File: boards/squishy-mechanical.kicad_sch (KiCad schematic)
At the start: 8 parts

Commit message: hardware: a bunch of clean up and the like
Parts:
- renumbered FID3 to FID1, FID1 to FID2, FID2 to FID3, FID5 to FID4, FID4 to FID5, G2 to G1, G1 to G2
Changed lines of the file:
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@@
   (symbol (lib_id "Mechanical:Fiducial") (at 17.78 17.78 0) (unit 1)
     (in_bom yes) (on_board yes)
-    (property "Reference" "FID1" (id 0) (at 19.939 16.6116 0)
+    (property "Reference" "FID2" (id 0) (at 19.939 16.6116 0)
       (effects (font (size 1.27 1.27)) (justify left))
     )
@@
   (symbol (lib_id "Mechanical:Fiducial") (at 17.78 22.86 0) (unit 1)
     (in_bom yes) (on_board yes)
-    (property "Reference" "FID2" (id 0) (at 19.939 21.6916 0)
+    (property "Reference" "FID3" (id 0) (at 19.939 21.6916 0)
       (effects (font (size 1.27 1.27)) (justify left))
     )
@@
   (symbol (lib_id "Mechanical:Fiducial") (at 17.78 27.94 0) (unit 1)
     (in_bom yes) (on_board yes)
-    (property "Reference" "FID3" (id 0) (at 19.939 26.7716 0)
+    (property "Reference" "FID1" (id 0) (at 19.939 26.7716 0)
       (effects (font (size 1.27 1.27)) (justify left))
     )
@@
   (symbol (lib_id "Mechanical:Fiducial") (at 30.48 17.78 0) (unit 1)
     (in_bom yes) (on_board yes)
-    (property "Reference" "FID4" (id 0) (at 32.639 16.6116 0)
+    (property "Reference" "FID5" (id 0) (at 32.639 16.6116 0)
       (effects (font (size 1.27 1.27)) (justify left))
     )
@@
   (symbol (lib_id "Mechanical:Fiducial") (at 30.48 22.86 0) (unit 1)
     (in_bom yes) (on_board yes)
-    (property "Reference" "FID5" (id 0) (at 32.639 21.6916 0)
+    (property "Reference" "FID4" (id 0) (at 32.639 21.6916 0)
       (effects (font (size 1.27 1.27)) (justify left))
     )
@@
   (symbol (lib_id "lethalbit-graphics:Graphic") (at 278.13 60.96 0) (unit 1)
     (in_bom yes) (on_board yes)
-    (property "Reference" "G2" (id 0) (at 278.13 57.15 0))
+    (property "Reference" "G1" (id 0) (at 278.13 57.15 0))
     (property "Value" "Graphic" (id 1) (at 278.13 64.77 0))
     (property "Footprint" "lethalbit-graphics:ran-filled" (id 2) (at 278.13 60.96 0)
@@
   (symbol (lib_id "lethalbit-graphics:Antifaschistische_Aktion") (at 358.14 12.7 0) (unit 1)
     (in_bom yes) (on_board yes)
-    (property "Reference" "G1" (id 0) (at 406.2222 61.1632 0)
+    (property "Reference" "G2" (id 0) (at 406.2222 61.1632 0)
       (effects (font (size 1.27 1.27)) (justify left) hide)
     )

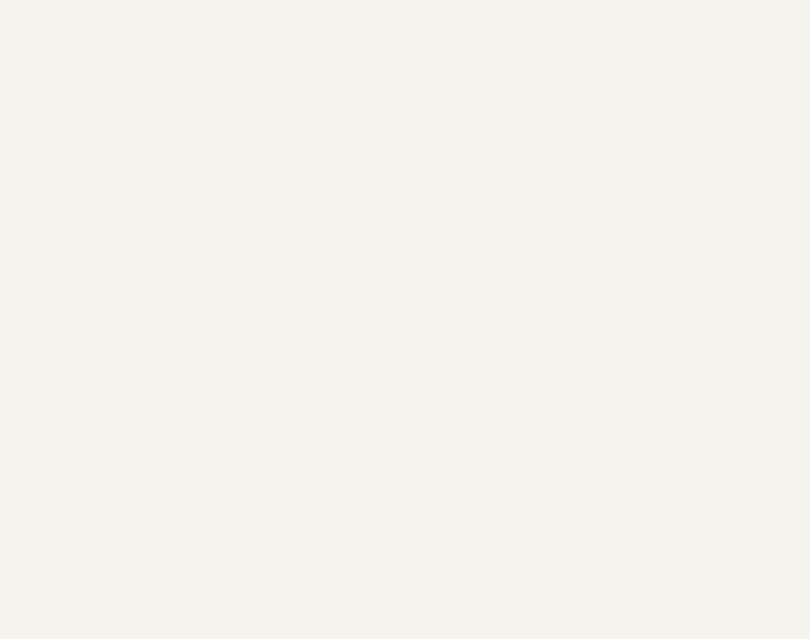
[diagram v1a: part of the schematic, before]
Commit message: hardware: fixed up some datasheets for symbols and added mounting holes
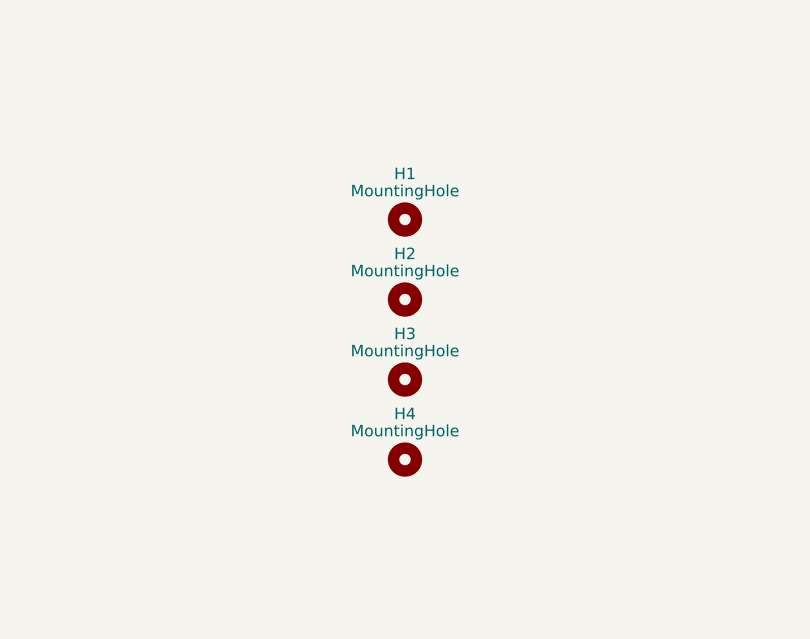
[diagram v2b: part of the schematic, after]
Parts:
- added H1, H2, H3, H4: MountingHole, MountingHole:MountingHole_3.2mm_M3, symbol Mechanical:MountingHole
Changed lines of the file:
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@@
+    )
+  )
+  (symbol (lib_id "Mechanical:MountingHole") (at 203.2 54.61 0) (unit 1)
+    (in_bom yes) (on_board yes)
+    (property "Reference" "H1" (id 0) (at 203.2 49.53 0))
+    (property "Value" "MountingHole" (id 1) (at 203.2 51.435 0))
+    (property "Footprint" "MountingHole:MountingHole_3.2mm_M3" (id 2) (at 203.2 54.61 0)
+      (effects (font (size 1.27 1.27)) hide)
+    )
+    (property "Datasheet" "~" (id 3) (at 203.2 54.61 0)
+      (effects (font (size 1.27 1.27)) hide)
+    )
+  )
+  (symbol (lib_id "Mechanical:MountingHole") (at 203.2 63.5 0) (unit 1)
+    (in_bom yes) (on_board yes)
+    (property "Reference" "H2" (id 0) (at 203.2 58.42 0))
+    (property "Value" "MountingHole" (id 1) (at 203.2 60.325 0))
+    (property "Footprint" "MountingHole:MountingHole_3.2mm_M3" (id 2) (at 203.2 63.5 0)
+      (effects (font (size 1.27 1.27)) hide)
+    )
+    (property "Datasheet" "~" (id 3) (at 203.2 63.5 0)
+      (effects (font (size 1.27 1.27)) hide)
+    )
+  )
+  (symbol (lib_id "Mechanical:MountingHole") (at 203.2 72.39 0) (unit 1)
+    (in_bom yes) (on_board yes)
+    (property "Reference" "H3" (id 0) (at 203.2 67.31 0))
+    (property "Value" "MountingHole" (id 1) (at 203.2 69.215 0))
+    (property "Footprint" "MountingHole:MountingHole_3.2mm_M3" (id 2) (at 203.2 72.39 0)
+      (effects (font (size 1.27 1.27)) hide)
+    )
+    (property "Datasheet" "~" (id 3) (at 203.2 72.39 0)
+      (effects (font (size 1.27 1.27)) hide)
+    )
+  )
+  (symbol (lib_id "Mechanical:MountingHole") (at 203.2 81.28 0) (unit 1)
+    (in_bom yes) (on_board yes)
+    (property "Reference" "H4" (id 0) (at 203.2 76.2 0))
+    (property "Value" "MountingHole" (id 1) (at 203.2 78.105 0))
+    (property "Footprint" "MountingHole:MountingHole_3.2mm_M3" (id 2) (at 203.2 81.28 0)
+      (effects (font (size 1.27 1.27)) hide)
+    )
+    (property "Datasheet" "~" (id 3) (at 203.2 81.28 0)
+      (effects (font (size 1.27 1.27)) hide)
     )
   )

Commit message: hardware: ensured all of the parts had a mpn and mfr
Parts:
- FID1, FID2, FID3, FID4, FID5, FID6, G1, G2, H1, H2, H3, H4: MFR (none) -> N/A; MPN (none) -> N/A
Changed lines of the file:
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@@
+      (effects (font (size 1.27 1.27)) hide)
+    )
+    (property "MFR" "N/A" (id 4) (at 17.78 17.78 0)
+      (effects (font (size 1.27 1.27)) hide)
+    )
+    (property "MPN" "N/A" (id 5) (at 17.78 17.78 0)
       (effects (font (size 1.27 1.27)) hide)
     )
@@
       (effects (font (size 1.27 1.27)) hide)
     )
+    (property "MFR" "N/A" (id 4) (at 17.78 22.86 0)
+      (effects (font (size 1.27 1.27)) hide)
+    )
+    (property "MPN" "N/A" (id 5) (at 17.78 22.86 0)
+      (effects (font (size 1.27 1.27)) hide)
+    )
   )
   (symbol (lib_id "Mechanical:Fiducial") (at 17.78 27.94 0) (unit 1)
@@
       (effects (font (size 1.27 1.27)) hide)
     )
+    (property "MFR" "N/A" (id 4) (at 17.78 27.94 0)
+      (effects (font (size 1.27 1.27)) hide)
+    )
+    (property "MPN" "N/A" (id 5) (at 17.78 27.94 0)
+      (effects (font (size 1.27 1.27)) hide)
+    )
   )
   (symbol (lib_id "Mechanical:Fiducial") (at 30.48 17.78 0) (unit 1)
@@
       (effects (font (size 1.27 1.27)) hide)
     )
+    (property "MFR" "N/A" (id 4) (at 30.48 17.78 0)
+      (effects (font (size 1.27 1.27)) hide)
+    )
+    (property "MPN" "N/A" (id 5) (at 30.48 17.78 0)
+      (effects (font (size 1.27 1.27)) hide)
+    )
   )
   (symbol (lib_id "Mechanical:Fiducial") (at 30.48 22.86 0) (unit 1)
@@
       (effects (font (size 1.27 1.27)) hide)
     )
+    (property "MFR" "N/A" (id 4) (at 30.48 22.86 0)
+      (effects (font (size 1.27 1.27)) hide)
+    )
+    (property "MPN" "N/A" (id 5) (at 30.48 22.86 0)
+      (effects (font (size 1.27 1.27)) hide)
+    )
   )
   (symbol (lib_id "Mechanical:Fiducial") (at 30.48 27.94 0) (unit 1)
@@
     )
     (property "Datasheet" "~" (id 3) (at 30.48 27.94 0)
+      (effects (font (size 1.27 1.27)) hide)
+    )
+    (property "MFR" "N/A" (id 4) (at 30.48 27.94 0)
+      (effects (font (size 1.27 1.27)) hide)
+    )
+    (property "MPN" "N/A" (id 5) (at 30.48 27.94 0)
       (effects (font (size 1.27 1.27)) hide)
     )
@@
       (effects (font (size 1.27 1.27)) hide)
     )
+    (property "MFR" "N/A" (id 4) (at 203.2 54.61 0)
+      (effects (font (size 1.27 1.27)) hide)
+    )
+    (property "MPN" "N/A" (id 5) (at 203.2 54.61 0)
+      (effects (font (size 1.27 1.27)) hide)
+    )
   )
   (symbol (lib_id "Mechanical:MountingHole") (at 203.2 63.5 0) (unit 1)
@@
       (effects (font (size 1.27 1.27)) hide)
     )
+    (property "MFR" "N/A" (id 4) (at 203.2 63.5 0)
+      (effects (font (size 1.27 1.27)) hide)
+    )
+    (property "MPN" "N/A" (id 5) (at 203.2 63.5 0)
+      (effects (font (size 1.27 1.27)) hide)
+    )
   )
   (symbol (lib_id "Mechanical:MountingHole") (at 203.2 72.39 0) (unit 1)
@@
       (effects (font (size 1.27 1.27)) hide)
     )
+    (property "MFR" "N/A" (id 4) (at 203.2 72.39 0)
+      (effects (font (size 1.27 1.27)) hide)
+    )
+    (property "MPN" "N/A" (id 5) (at 203.2 72.39 0)
+      (effects (font (size 1.27 1.27)) hide)
+    )
   )
   (symbol (lib_id "Mechanical:MountingHole") (at 203.2 81.28 0) (unit 1)
@@
       (effects (font (size 1.27 1.27)) hide)
     )
+    (property "MFR" "N/A" (id 4) (at 203.2 81.28 0)
+      (effects (font (size 1.27 1.27)) hide)
+    )
+    (property "MPN" "N/A" (id 5) (at 203.2 81.28 0)
+      (effects (font (size 1.27 1.27)) hide)
+    )
   )
   (symbol (lib_id "lethalbit-graphics:Graphic") (at 278.13 60.96 0) (unit 1)
@@
       (effects (font (size 1.27 1.27)) hide)
     )
+    (property "MFR" "N/A" (id 4) (at 278.13 60.96 0)
+      (effects (font (size 1.27 1.27)) hide)
+    )
+    (property "MPN" "N/A" (id 5) (at 278.13 60.96 0)
+      (effects (font (size 1.27 1.27)) hide)
+    )
   )
   (symbol (lib_id "lethalbit-graphics:Antifaschistische_Aktion") (at 358.14 12.7 0) (unit 1)
@@
       (effects (font (size 1.27 1.27)) hide)
     )
+    (property "MFR" "N/A" (id 4) (at 358.14 12.7 0)
+      (effects (font (size 1.27 1.27)) hide)
+    )
+    (property "MPN" "N/A" (id 5) (at 358.14 12.7 0)
+      (effects (font (size 1.27 1.27)) hide)
+    )
